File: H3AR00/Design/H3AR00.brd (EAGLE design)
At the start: 50.8 x 45.6 mm, 8 parts, among them P1 HEXABIT_18.00_REVERSED, U1 TPS76433DBVT

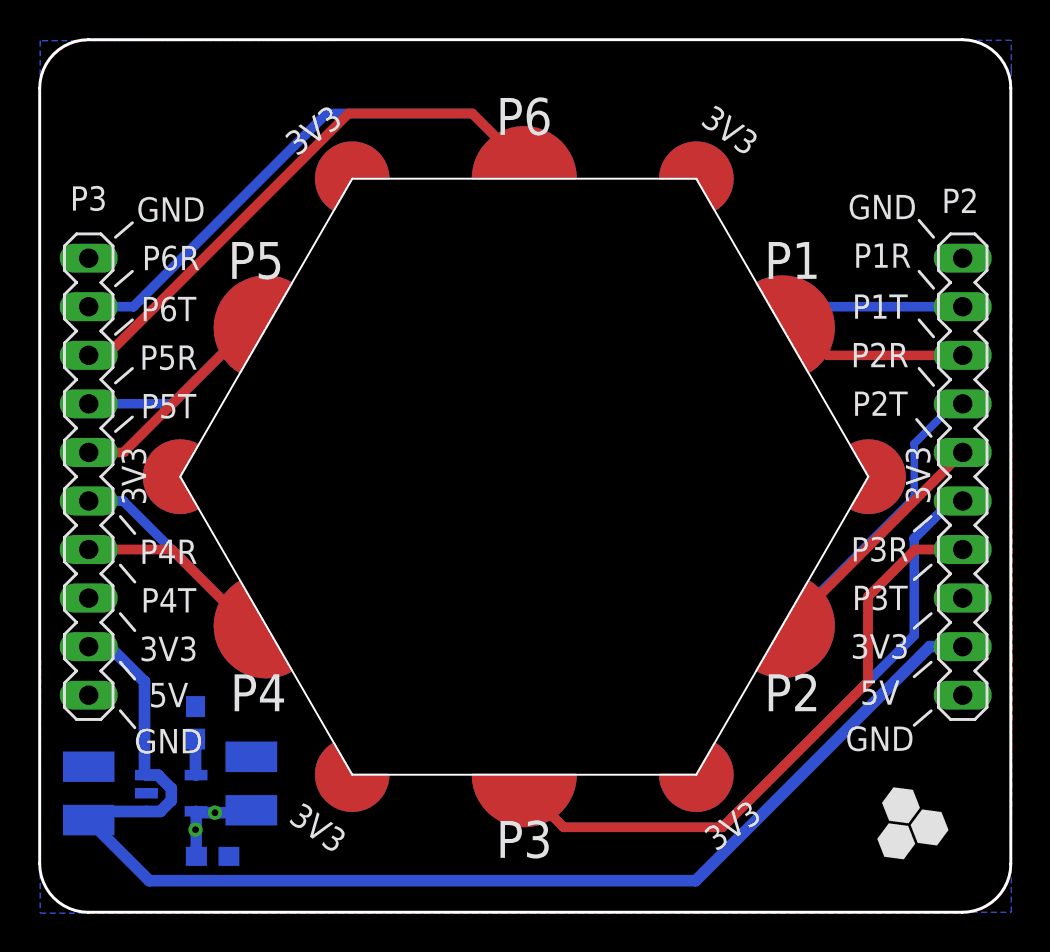
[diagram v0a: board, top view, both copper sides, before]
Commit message: Reduce module opening from side 18mm to side 17.6mm Revision 1
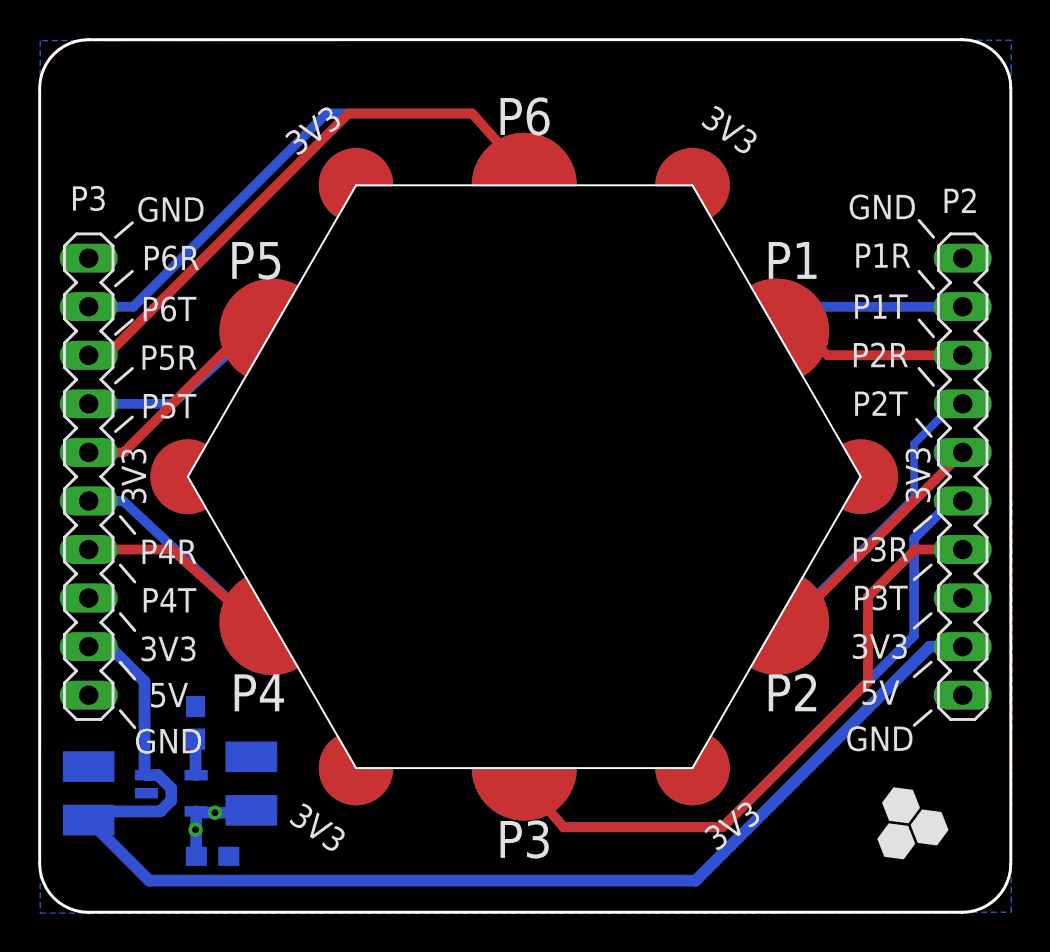
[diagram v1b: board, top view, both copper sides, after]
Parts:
- P1: value HEXABIT_18.00_REVERSED -> HEXABIT_17.60_REVERSED; device hexabitz_connectors:HEXABIT_18.00_REVERSED -> hexabitz_connectors:HEXABIT_17.60_REVERSED
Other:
- board text added: "H3AR01"
- board text removed: "H3AR00"
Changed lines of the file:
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@@
 <?xml version="1.0" encoding="utf-8"?>
 <!DOCTYPE eagle SYSTEM "eagle.dtd">
-<eagle version="9.3.0">
+<eagle version="9.6.1">
 <drawing>
 <settings>
@@
 <text x="35.99" y="54.836" size="1.9304" layer="21" font="vector" align="center">P6</text>
 <text x="35.99" y="54.836" size="1.9304" layer="22" font="vector" rot="MR0" align="center">P6</text>
-<text x="54.2798" y="20.76881875" size="1.9304" layer="22" font="vector" rot="MR0" align="center">H3AR00</text>
+<text x="54.2798" y="20.76881875" size="1.9304" layer="22" font="vector" rot="MR0" align="center">H3AR01</text>
 <rectangle x1="55.83046875" y1="15.969996875" x2="55.8452" y2="15.984728125" layer="21"/>
 <rectangle x1="55.712615625" y1="15.984728125" x2="55.859934375" y2="15.999459375" layer="21"/>
@@
 </autorouter>
 <elements>
-<element name="P1" library="hexabitz_connectors" package="HEXABIT_18.00_REVERSED" value="HEXABIT_18.00_REVERSED" x="35.9918" y="35.9918" smashed="yes"/>
+<element name="P1" library="hexabitz_connectors" library_urn="urn:adsk.eagle:library:20064578" package="HEXABIT_17.60_REVERSED" package3d_urn="urn:adsk.eagle:package:20064623/4" value="HEXABIT_17.60_REVERSED" x="35.9918" y="35.9918" smashed="yes"/>
 <element name="P2" library="Hexabitz" package="MA10-1" package3d_urn="urn:adsk.eagle:package:8346/1" value="" x="58.928" y="35.9918" locked="yes" smashed="yes" rot="R90">
 <attribute name="MF" value="" x="58.928" y="35.9918" size="1.778" layer="27" rot="R90" display="off"/>
@@
 <contactref element="P2" pad="8"/>
 <wire x1="58.928" y1="42.3418" x2="51.8718" y2="42.3418" width="0.508" layer="1"/>
-<wire x1="51.8718" y1="42.3418" x2="50.0918" y2="44.1218" width="0.508" layer="1"/>
+<wire x1="51.8718" y1="42.3418" x2="49.7918" y2="43.94855" width="0.508" layer="1"/>
 </signal>
 <signal name="P1_RXD">
@@
 <contactref element="P2" pad="9"/>
 <wire x1="58.928" y1="44.8818" x2="50.8518" y2="44.8818" width="0.508" layer="16"/>
-<wire x1="50.8518" y1="44.8818" x2="50.0918" y2="44.1218" width="0.508" layer="16"/>
+<wire x1="50.8518" y1="44.8818" x2="49.7918" y2="43.94855" width="0.508" layer="16"/>
 </signal>
 <signal name="P2_TXD">
@@
 <contactref element="P1" pad="PAD_PU2"/>
 <wire x1="58.928" y1="37.2618" x2="50.0918" y2="28.4256" width="0.508" layer="1"/>
-<wire x1="50.0918" y1="28.4256" x2="50.0918" y2="27.8618" width="0.508" layer="1"/>
+<wire x1="50.0918" y1="28.4256" x2="49.7918" y2="28.03505" width="0.508" layer="1"/>
 </signal>
 <signal name="P2_RXD">
@@
 <wire x1="58.928" y1="39.8018" x2="58.4708" y2="39.8018" width="0.508" layer="16"/>
 <wire x1="56.388" y1="34.92" x2="50.0918" y2="28.6238" width="0.4064" layer="16"/>
-<wire x1="50.0918" y1="28.6238" x2="50.0918" y2="27.8618" width="0.508" layer="16"/>
+<wire x1="50.0918" y1="28.6238" x2="49.7918" y2="28.03505" width="0.508" layer="16"/>
 <wire x1="58.4708" y1="39.8018" x2="56.388" y2="37.719" width="0.4064" layer="16"/>
 <wire x1="56.388" y1="37.719" x2="56.388" y2="34.92" width="0.4064" layer="16"/>
@@
 <wire x1="56.4388" y1="32.1818" x2="53.975" y2="29.718" width="0.508" layer="1"/>
 <wire x1="53.975" y1="29.718" x2="53.975" y2="25.273" width="0.508" layer="1"/>
-<wire x1="38.0506" y1="17.653" x2="35.9918" y2="19.7118" width="0.508" layer="1"/>
+<wire x1="38.0506" y1="17.653" x2="35.9918" y2="20.0583" width="0.508" layer="1"/>
 <wire x1="53.975" y1="25.273" x2="46.355" y2="17.653" width="0.508" layer="1"/>
 <wire x1="46.355" y1="17.653" x2="38.0506" y2="17.653" width="0.508" layer="1"/>
@@
 <contactref element="P1" pad="PAD_PD3"/>
 <contactref element="P2" pad="5"/>
-<wire x1="35.9918" y1="19.7118" x2="38.0506" y2="17.653" width="0.508" layer="16"/>
+<wire x1="35.9918" y1="20.0583" x2="38.0506" y2="17.653" width="0.508" layer="16"/>
 <wire x1="56.388" y1="27.686" x2="56.388" y2="32.766" width="0.508" layer="16"/>
 <wire x1="56.388" y1="32.766" x2="58.3438" y2="34.7218" width="0.508" layer="16"/>
@@
 <contactref element="P1" pad="PAD_PU4"/>
 <wire x1="13.208" y1="32.1818" x2="17.5518" y2="32.1818" width="0.508" layer="1"/>
-<wire x1="17.5518" y1="32.1818" x2="21.8918" y2="27.8418" width="0.508" layer="1"/>
+<wire x1="17.5518" y1="32.1818" x2="22.1918" y2="28.01505" width="0.508" layer="1"/>
 </signal>
 <signal name="P4_RXD">
@@
 <contactref element="P1" pad="PAD_PD4"/>
 <wire x1="13.208" y1="34.7218" x2="15.0118" y2="34.7218" width="0.508" layer="16"/>
-<wire x1="15.0118" y1="34.7218" x2="21.8918" y2="27.8418" width="0.508" layer="16"/>
+<wire x1="15.0118" y1="34.7218" x2="22.1918" y2="28.01505" width="0.508" layer="16"/>
 </signal>
 <signal name="P5_TXD">
@@
 <contactref element="P1" pad="PAD_PU5"/>
 <wire x1="13.208" y1="37.2618" x2="15.0368" y2="37.2618" width="0.508" layer="1"/>
-<wire x1="21.8918" y1="44.1218" x2="21.8918" y2="44.1168" width="0.508" layer="1"/>
+<wire x1="22.1918" y1="43.94855" x2="21.8918" y2="44.1168" width="0.508" layer="1"/>
 <wire x1="21.8918" y1="44.1168" x2="15.0368" y2="37.2618" width="0.508" layer="1"/>
 </signal>
@@
 <contactref element="P1" pad="PAD_PD5"/>
 <wire x1="13.208" y1="39.8018" x2="17.5718" y2="39.8018" width="0.508" layer="16"/>
-<wire x1="17.5718" y1="39.8018" x2="21.8918" y2="44.1218" width="0.508" layer="16"/>
+<wire x1="17.5718" y1="39.8018" x2="22.1918" y2="43.94855" width="0.508" layer="16"/>
 </signal>
 <signal name="P6_TXD">
@@
 <contactref element="P1" pad="PAD_PU6"/>
 <wire x1="13.208" y1="42.3418" x2="14.1478" y2="42.3418" width="0.508" layer="1"/>
-<wire x1="33.2726" y1="54.991" x2="35.9918" y2="52.2718" width="0.508" layer="1"/>
+<wire x1="33.2726" y1="54.991" x2="35.9918" y2="51.9253" width="0.508" layer="1"/>
 <wire x1="14.1478" y1="42.3418" x2="26.797" y2="54.991" width="0.508" layer="1"/>
 <wire x1="26.797" y1="54.991" x2="33.2726" y2="54.991" width="0.508" layer="1"/>
@@
 <wire x1="15.5448" y1="44.8818" x2="25.654" y2="54.991" width="0.508" layer="16"/>
 <wire x1="25.654" y1="54.991" x2="33.2726" y2="54.991" width="0.508" layer="16"/>
-<wire x1="33.2726" y1="54.991" x2="35.9918" y2="52.2718" width="0.508" layer="16"/>
+<wire x1="33.2726" y1="54.991" x2="35.9918" y2="51.9253" width="0.4064" layer="16"/>
 </signal>
 <signal name="N$1">
@@
 </drawing>
 <compatibility>
+<note version="8.2" severity="warning">
+Since Version 8.2, EAGLE supports online libraries. The ids
+of those online libraries will not be understood (or retained)
+with this version.
+</note>
 <note version="8.3" severity="warning">
 Since Version 8.3, EAGLE supports URNs for individual library
